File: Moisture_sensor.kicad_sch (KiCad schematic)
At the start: 3 parts, among them J1 Conn_01x02_Socket, U2 TLV2371DBV

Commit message: Completed first iteration and reviews
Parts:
- added C19, C23: 100nF, Capacitor_SMD:C_0805_2012Metric_Pad1.18x1.45mm_HandSolder, symbol Device:C
- added D2: BZX84C3V3-7-F, Package_TO_SOT_SMD:SOT-23, symbol Diode:BZX84Cxx
- added R11: 500k, Resistor_SMD:R_0805_2012Metric_Pad1.20x1.40mm_HandSolder, symbol Device:R
- added R6: 100, Resistor_SMD:R_0805_2012Metric_Pad1.20x1.40mm_HandSolder, symbol Device:R
- added SenseOut1, Vsense1: TestPoint, TestPoint:TestPoint_Pad_D1.0mm, symbol Connector:TestPoint
- J1: footprint (none) -> Connector_Wire:SolderWire-0.1sqmm_1x02_P3.6mm_D0.4mm_OD1mm_Relief
- R1: value 100k -> 500k; footprint (none) -> Resistor_SMD:R_0805_2012Metric_Pad1.20x1.40mm_HandSolder; Supplier (none) -> Digikey; Supplier Part Number (none) -> 738-RNCF0805BTE500KCT-ND
- U2: Supplier (none) -> Digikey; Supplier Part Number (none) -> 296-13057-1-ND
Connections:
- net GND: now also C19.2, C23.2, D2.1 (A), R11.1
- net OP_AMP_POWER: now also C23.1, R11.2
- net SENSOR_OUTPUT: now also C19.1, R6.2, SenseOut1.1; no longer U2.1, U2.4 (-)
- net Vsens: now reaches J1.1 (Pin_1), R1.1, U2.3 (+)
- net Vsens: now also D2.3 (K), Vsense1.1
- new net: R6.1, U2.1, U2.4 (-)
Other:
- note added: "Pulldown to ensure off, when unpowered"
- company: (none) -> Horatio Pistachio
- title: (none) -> WashingLineMonitor-P0001
- moved on the sheet: J1

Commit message: commit of local files before designing next version
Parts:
- D2: JLC_Part_Number (none) -> C177019
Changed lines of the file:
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@@
+			)
+		)
+		(property "JLC_Part_Number" ""
+			(at 193.04 88.9 90)
+			(effects
+				(font
+					(size 1.27 1.27)
+				)
+				(hide yes)
 			)
 		)
@@
 		)
 		(property "Supplier Part Number" "BZX84C3V3-FDICT-ND"
+			(at 105.41 96.52 90)
+			(effects
+				(font
+					(size 1.27 1.27)
+				)
+				(hide yes)
+			)
+		)
+		(property "JLC_Part_Number" "C177019"
 			(at 105.41 96.52 90)
 			(effects
@@
 			)
 		)
+		(property "JLC_Part_Number" ""
+			(at 123.19 85.09 0)
+			(effects
+				(font
+					(size 1.27 1.27)
+				)
+				(hide yes)
+			)
+		)
 		(pin "1"
 		)
@@
 			)
 		)
+		(property "JLC_Part_Number" ""
+			(at 199.39 64.77 0)
+			(effects
+				(font
+					(size 1.27 1.27)
+				)
+				(hide yes)
+			)
+		)
 		(pin "1"
 		)
@@
 		)
 		(property "Supplier" "Digikey"
+			(at 170.18 88.9 0)
+			(effects
+				(font
+					(size 1.27 1.27)
+				)
+				(hide yes)
+			)
+		)
+		(property "JLC_Part_Number" ""
 			(at 170.18 88.9 0)
 			(effects
@@
 			)
 		)
+		(property "JLC_Part_Number" ""
+			(at 212.09 88.9 0)
+			(effects
+				(font
+					(size 1.27 1.27)
+				)
+				(hide yes)
+			)
+		)
 		(pin "1"
 		)
@@
 			)
 		)
+		(property "JLC_Part_Number" ""
+			(at 177.8 66.04 0)
+			(effects
+				(font
+					(size 1.27 1.27)
+				)
+				(hide yes)
+			)
+		)
 		(pin "1"
 		)
@@
 			)
 		)
+		(property "JLC_Part_Number" ""
+			(at 199.39 92.71 0)
+			(effects
+				(font
+					(size 1.27 1.27)
+				)
+				(hide yes)
+			)
+		)
 		(pin "1"
 		)
@@
 		)
 		(property "Description" "test point"
+			(at 140.97 86.36 0)
+			(effects
+				(font
+					(size 1.27 1.27)
+				)
+				(hide yes)
+			)
+		)
+		(property "JLC_Part_Number" ""
 			(at 140.97 86.36 0)
 			(effects
@@
 			(at 80.01 92.71 0)
 			(effects
+				(font
+					(size 1.27 1.27)
+				)
+				(hide yes)
+			)
+		)
+		(property "JLC_Part_Number" ""
+			(at 80.01 92.71 0)
+			(effects

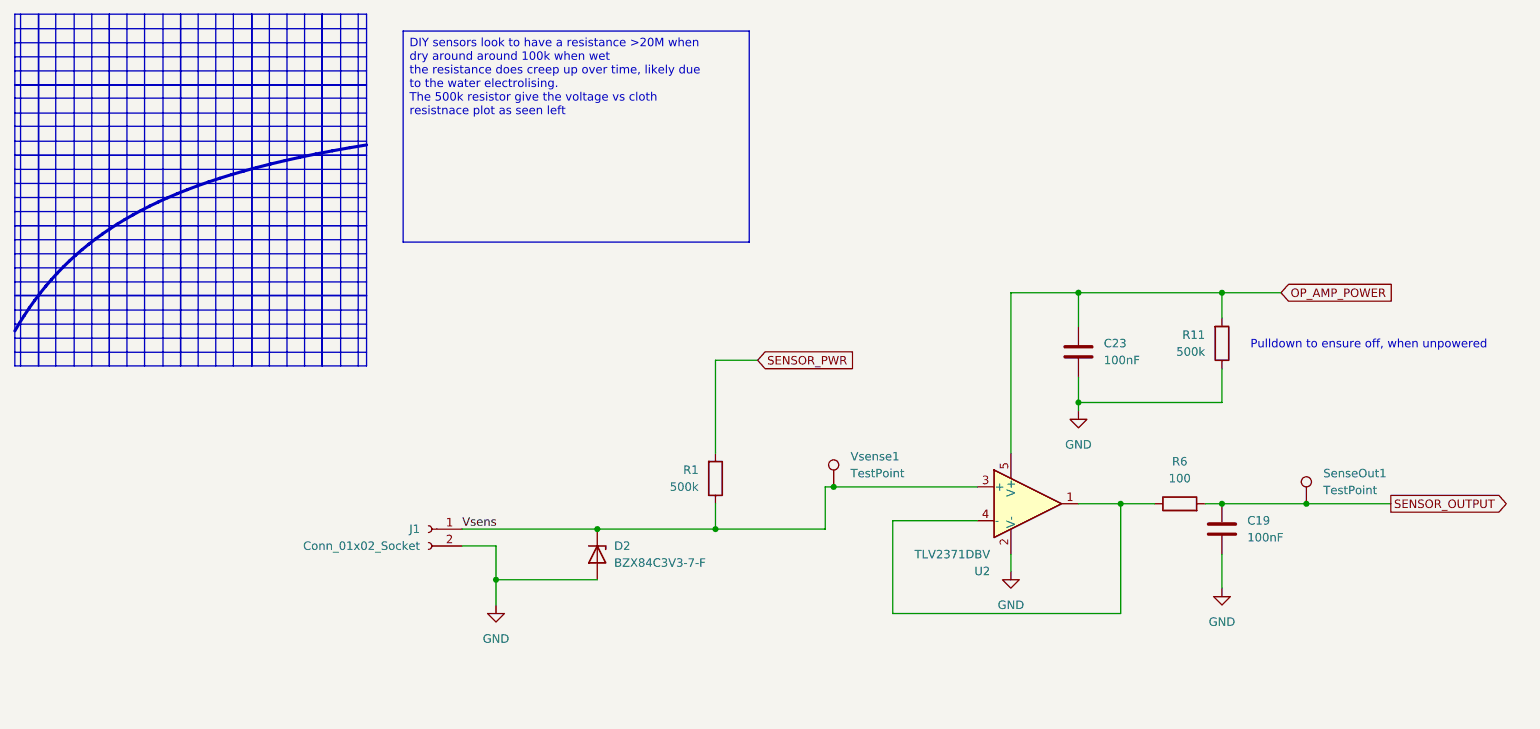
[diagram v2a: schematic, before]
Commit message: updated schematic from review
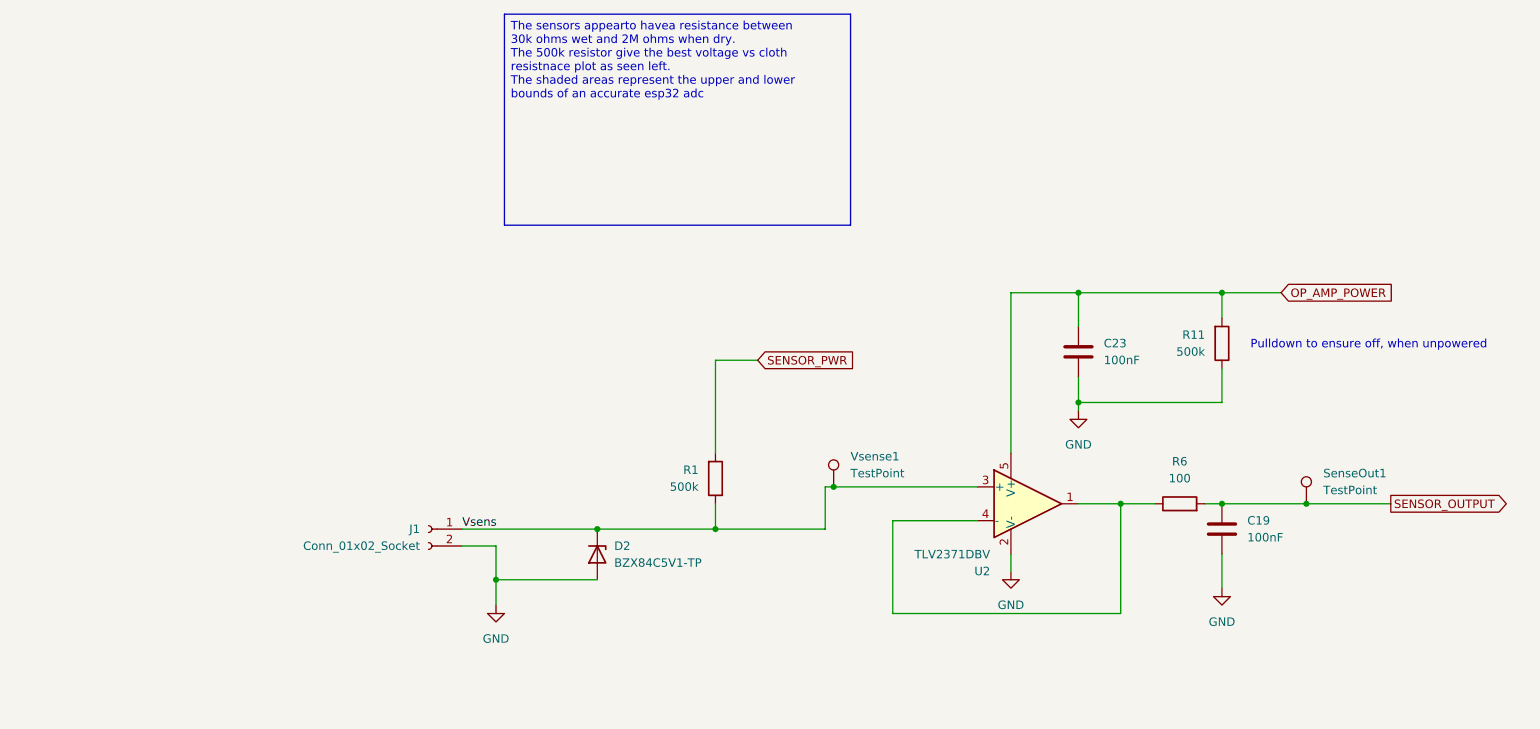
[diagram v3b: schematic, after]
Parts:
- D2: value BZX84C3V3-7-F -> BZX84C5V1-TP; JLC_Part_Number C177019 -> (none); Supplier Part Number BZX84C3V3-FDICT-ND -> BZX84C5V1-TPMSCT-ND

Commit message: laid out pcb
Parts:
- removed J1: Conn_01x02_Socket, Connector_Wire:SolderWire-0.1sqmm_1x02_P3.6mm_D0.4mm_OD1mm_Relief, symbol Connector:Conn_01x02_Socket
- added J1, J2: S1711-46R, Hydro_footprints:HARWIN_S1711-46R, symbol Hydro_symbols:S1711-46R
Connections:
- net GND: now also J2.SH1 (SHIELD)
- net Vsens: now also J1.SH1 (SHIELD)
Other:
- moved on the sheet: D2

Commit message: Near complete AC
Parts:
- renumbered Vsense1 to TP1, SenseOut1 to TP2
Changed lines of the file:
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@@
 		(dnp no)
 		(fields_autoplaced yes)
-		(property "Reference" "SenseOut1"
+		(property "Reference" "TP2"
 			(at 214.63 84.3279 0)
 			(show_name no)
@@
 			(project "WashingLineMonitor-P0001"
 				(path "/09468f75-1295-4aed-9d66-1cbb46f6d9f7/85e6dc6f-9ecf-46c8-b531-16bea54980b8"
-					(reference "SenseOut1")
+					(reference "TP2")
 					(unit 1)
 				)
@@
 		(dnp no)
 		(fields_autoplaced yes)
-		(property "Reference" "Vsense1"
+		(property "Reference" "TP1"
 			(at 143.51 81.7879 0)
 			(show_name no)
@@
 			(project "WashingLineMonitor-P0001"
 				(path "/09468f75-1295-4aed-9d66-1cbb46f6d9f7/85e6dc6f-9ecf-46c8-b531-16bea54980b8"
-					(reference "Vsense1")
+					(reference "TP1")
 					(unit 1)
 				)

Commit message: Minor pre release changes
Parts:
- TP1, TP2: now left out of the parts list
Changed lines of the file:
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@@
 	(title_block
 		(title "WashingLineMonitor-P0001")
-		(date "2025-09-14")
-		(rev "AB")
+		(date "2026-06-06")
+		(rev "AC")
 		(company "Horatio Pistachio")
 	)
@@
 		(body_style 1)
 		(exclude_from_sim no)
-		(in_bom yes)
+		(in_bom no)
 		(on_board yes)
 		(in_pos_files yes)
@@
 		(body_style 1)
 		(exclude_from_sim no)
-		(in_bom yes)
+		(in_bom no)
 		(on_board yes)
 		(in_pos_files yes)
